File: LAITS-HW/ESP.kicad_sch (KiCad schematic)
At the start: 53 parts, among them J501 JTAG, SW501 SW_BOOT, SW502 SW_RST, SW503 SW_LOG_SD_EN, SW504 SW_RST_PROV, SW505 SW_RGB_CHRG, SW506 SW_SLEEP, U501 ESP32-WROVER-IE/E, U502 SX1503I091TRT

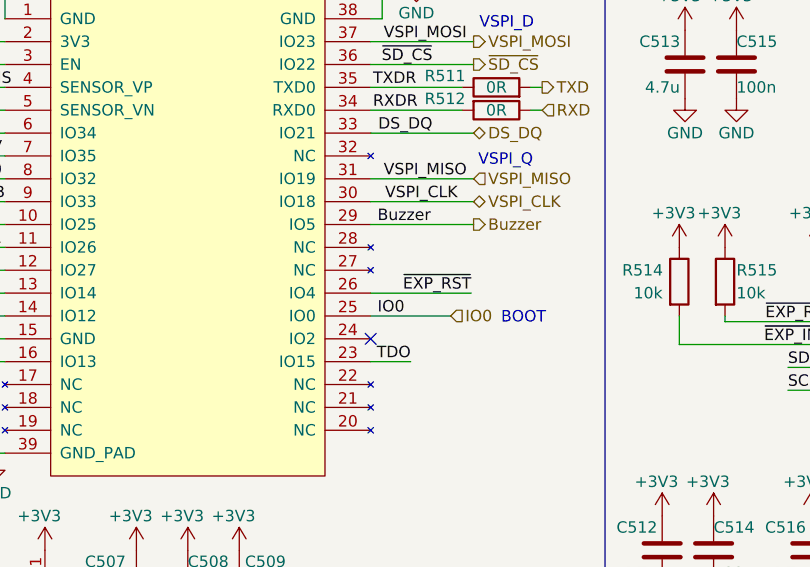
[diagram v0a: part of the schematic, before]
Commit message: improved silkscreen placement and some minor changes
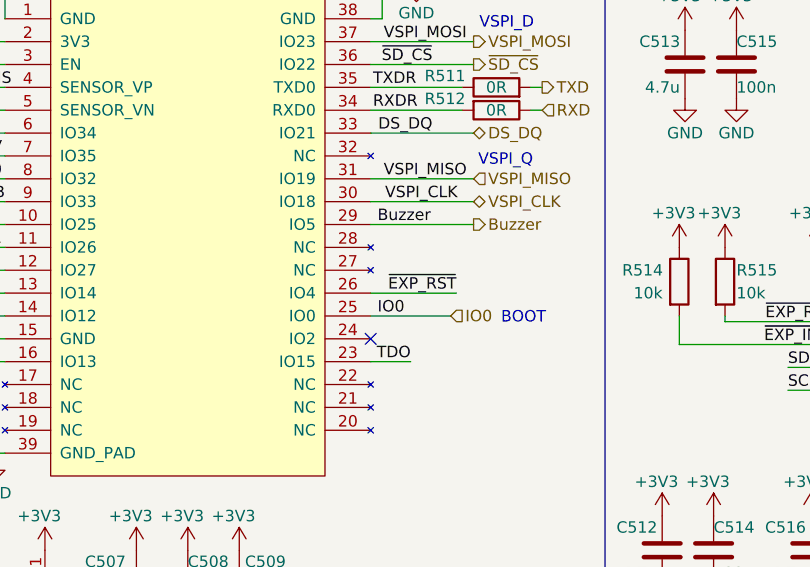
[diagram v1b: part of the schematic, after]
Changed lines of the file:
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@@
     (stroke (width 0) (type default) (color 0 0 0 0))
   )
-  (wire (pts (xy 161.29 59.69) (xy 172.466 59.69))
+  (wire (pts (xy 161.29 59.69) (xy 170.815 59.69))
     (stroke (width 0) (type default) (color 0 0 0 0))
   )
@@
     (effects (font (size 1.27 1.27)) (justify right bottom))
   )
-  (label "~{EXP_RST}" (at 172.466 59.69 180)
-    (effects (font (size 1.27 1.27)) (justify right bottom))
-  )
+  (label "~{EXP_RST}" (at 170.815 59.69 180)
+    (effects (font (size 1.27 1.27)) (justify right bottom))
+  )

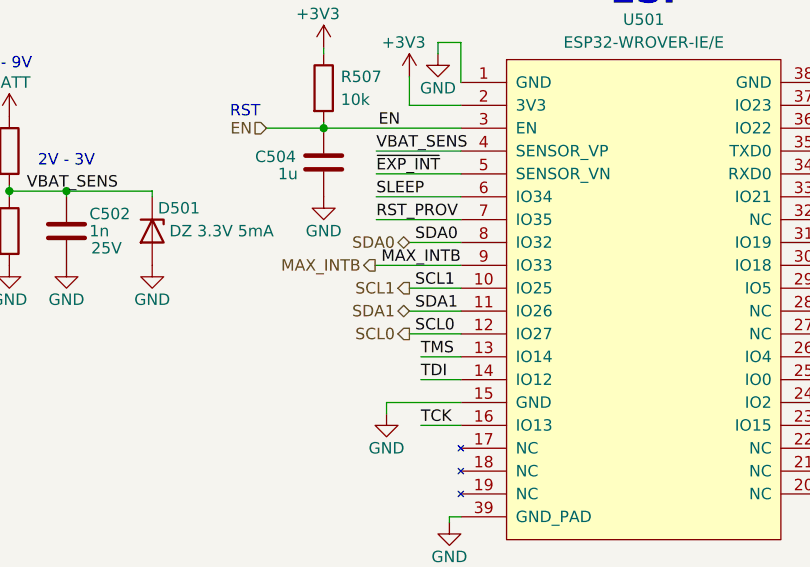
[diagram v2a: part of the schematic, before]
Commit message: Fixed a minor bug in the assignment of SDA0 and SCL0 pins, doesn't affect Hardware, swap in firmware
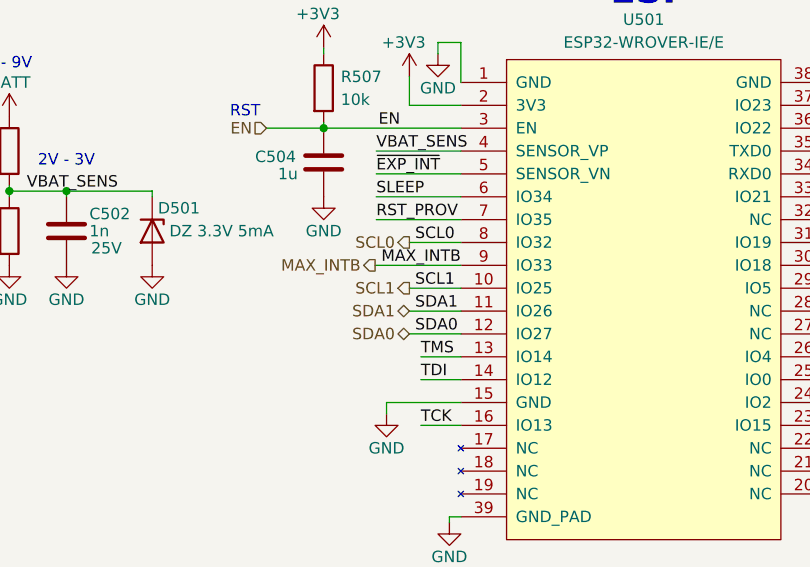
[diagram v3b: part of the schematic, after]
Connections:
- net SCL0: now also U501.8 (IO32); no longer U501.12 (IO27)
- net SDA0: now also U501.12 (IO27); no longer U501.8 (IO32)
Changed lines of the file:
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@@
   (title_block
     (title "ESP")
-    (date "2022-07-14")
-    (rev "1.0.1")
+    (date "2022-08-11")
+    (rev "1.0.2")
     (company "Simone Tollardo")
   )
@@
     (stroke (width 0) (type default) (color 0 0 0 0))
   )
+  (wire (pts (xy 114.935 57.15) (xy 120.65 57.15))
+    (stroke (width 0) (type default) (color 0 0 0 0))
+  )
   (wire (pts (xy 94.615 147.32) (xy 98.425 147.32))
     (stroke (width 0) (type default) (color 0 0 0 0))
@@
     (stroke (width 0) (type default) (color 0 0 0 0))
   )
+  (wire (pts (xy 120.65 24.765) (xy 120.65 29.21))
+    (stroke (width 0) (type default) (color 0 0 0 0))
+  )
+  (wire (pts (xy 154.305 147.32) (xy 154.305 150.495))
+    (stroke (width 0) (type default) (color 0 0 0 0))
+  )
+  (polyline (pts (xy 236.22 137.795) (xy 236.22 143.51))
+    (stroke (width 0) (type default) (color 0 0 0 0))
+  )
+  (wire (pts (xy 207.645 67.945) (xy 212.725 67.945))
+    (stroke (width 0) (type default) (color 0 0 0 0))
+  )
+  (wire (pts (xy 158.115 147.32) (xy 158.115 144.78))
+    (stroke (width 0) (type default) (color 0 0 0 0))
+  )
+  (wire (pts (xy 161.29 29.21) (xy 162.56 29.21))
+    (stroke (width 0) (type default) (color 0 0 0 0))
+  )
+  (wire (pts (xy 136.525 123.19) (xy 136.525 124.46))
+    (stroke (width 0) (type default) (color 0 0 0 0))
+  )
+  (wire (pts (xy 238.125 37.465) (xy 248.285 37.465))
+    (stroke (width 0) (type default) (color 0 0 0 0))
+  )
+  (polyline (pts (xy 187.325 163.83) (xy 187.325 102.235))
+    (stroke (width 0) (type default) (color 0 0 0 0))
+  )
+  (polyline (pts (xy 236.22 143.51) (xy 283.21 143.51))
+    (stroke (width 0) (type default) (color 0 0 0 0))
+  )
+  (polyline (pts (xy 62.865 163.83) (xy 62.865 194.31))
+    (stroke (width 0) (type default) (color 0 0 0 0))
+  )
+  (wire (pts (xy 235.585 36.83) (xy 235.585 45.085))
+    (stroke (width 0) (type default) (color 0 0 0 0))
+  )
+  (wire (pts (xy 73.66 136.525) (xy 73.66 133.35))
+    (stroke (width 0) (type default) (color 0 0 0 0))
+  )
+  (wire (pts (xy 132.08 147.32) (xy 134.62 147.32))
+    (stroke (width 0) (type default) (color 0 0 0 0))
+  )
+  (wire (pts (xy 235.585 81.28) (xy 238.125 81.28))
+    (stroke (width 0) (type default) (color 0 0 0 0))
+  )
+  (wire (pts (xy 243.205 41.275) (xy 243.205 45.085))
+    (stroke (width 0) (type default) (color 0 0 0 0))
+  )
+  (wire (pts (xy 247.65 41.275) (xy 243.205 41.275))
+    (stroke (width 0) (type default) (color 0 0 0 0))
+  )
+  (wire (pts (xy 154.305 147.32) (xy 158.115 147.32))
+    (stroke (width 0) (type default) (color 0 0 0 0))
+  )
+  (wire (pts (xy 172.085 147.32) (xy 174.625 147.32))
+    (stroke (width 0) (type default) (color 0 0 0 0))
+  )
+  (wire (pts (xy 37.465 67.31) (xy 37.465 69.85))
+    (stroke (width 0) (type default) (color 0 0 0 0))
+  )
+  (wire (pts (xy 156.21 123.19) (xy 156.21 124.46))
+    (stroke (width 0) (type default) (color 0 0 0 0))
+  )
+  (polyline (pts (xy 283.21 164.465) (xy 190.5 164.465))
+    (stroke (width 0) (type default) (color 0 0 0 0))
+  )
+  (wire (pts (xy 238.125 45.085) (xy 238.125 37.465))
+    (stroke (width 0) (type default) (color 0 0 0 0))
+  )
+  (polyline (pts (xy 236.22 143.51) (xy 236.22 156.845))
+    (stroke (width 0) (type default) (color 0 0 0 0))
+  )
+  (wire (pts (xy 236.22 36.83) (xy 235.585 36.83))
+    (stroke (width 0) (type default) (color 0 0 0 0))
+  )
+  (wire (pts (xy 31.115 121.285) (xy 38.735 121.285))
+    (stroke (width 0) (type default) (color 0 0 0 0))
+  )
+  (polyline (pts (xy 62.865 13.97) (xy 62.865 102.235))
+    (stroke (width 0) (type default) (color 0 0 0 0))
+  )
+  (wire (pts (xy 161.29 31.75) (xy 172.72 31.75))
+    (stroke (width 0) (type default) (color 0 0 0 0))
+  )
+  (wire (pts (xy 80.01 147.32) (xy 80.01 144.78))
+    (stroke (width 0) (type default) (color 0 0 0 0))
+  )
+  (wire (pts (xy 76.835 41.275) (xy 76.835 41.91))
+    (stroke (width 0) (type default) (color 0 0 0 0))
+  )
+  (wire (pts (xy 156.21 133.35) (xy 158.115 133.35))
+    (stroke (width 0) (type default) (color 0 0 0 0))
+  )
+  (polyline (pts (xy 13.97 13.97) (xy 13.97 102.235))
+    (stroke (width 0) (type default) (color 0 0 0 0))
+  )
+  (wire (pts (xy 99.06 34.29) (xy 105.41 34.29))
+    (stroke (width 0) (type default) (color 0 0 0 0))
+  )
+  (wire (pts (xy 73.66 144.145) (xy 73.66 147.32))
+    (stroke (width 0) (type default) (color 0 0 0 0))
+  )
+  (wire (pts (xy 132.08 144.145) (xy 132.08 147.32))
+    (stroke (width 0) (type default) (color 0 0 0 0))
+  )
+  (wire (pts (xy 31.115 118.745) (xy 38.735 118.745))
+    (stroke (width 0) (type default) (color 0 0 0 0))
+  )
   (wire (pts (xy 114.935 46.99) (xy 120.65 46.99))
-    (stroke (width 0) (type default) (color 0 0 0 0))
-  )
-  (wire (pts (xy 120.65 24.765) (xy 120.65 29.21))
-    (stroke (width 0) (type default) (color 0 0 0 0))
-  )
-  (wire (pts (xy 154.305 147.32) (xy 154.305 150.495))
-    (stroke (width 0) (type default) (color 0 0 0 0))
-  )
-  (polyline (pts (xy 236.22 137.795) (xy 236.22 143.51))
-    (stroke (width 0) (type default) (color 0 0 0 0))
-  )
-  (wire (pts (xy 207.645 67.945) (xy 212.725 67.945))
-    (stroke (width 0) (type default) (color 0 0 0 0))
-  )
-  (wire (pts (xy 158.115 147.32) (xy 158.115 144.78))
-    (stroke (width 0) (type default) (color 0 0 0 0))
-  )
-  (wire (pts (xy 161.29 29.21) (xy 162.56 29.21))
-    (stroke (width 0) (type default) (color 0 0 0 0))
-  )
-  (wire (pts (xy 136.525 123.19) (xy 136.525 124.46))
-    (stroke (width 0) (type default) (color 0 0 0 0))
-  )
-  (wire (pts (xy 238.125 37.465) (xy 248.285 37.465))
-    (stroke (width 0) (type default) (color 0 0 0 0))
-  )
-  (polyline (pts (xy 187.325 163.83) (xy 187.325 102.235))
-    (stroke (width 0) (type default) (color 0 0 0 0))
-  )
-  (polyline (pts (xy 236.22 143.51) (xy 283.21 143.51))
-    (stroke (width 0) (type default) (color 0 0 0 0))
-  )
-  (polyline (pts (xy 62.865 163.83) (xy 62.865 194.31))
-    (stroke (width 0) (type default) (color 0 0 0 0))
-  )
-  (wire (pts (xy 235.585 36.83) (xy 235.585 45.085))
-    (stroke (width 0) (type default) (color 0 0 0 0))
-  )
-  (wire (pts (xy 114.935 57.15) (xy 120.65 57.15))
-    (stroke (width 0) (type default) (color 0 0 0 0))
-  )
-  (wire (pts (xy 73.66 136.525) (xy 73.66 133.35))
-    (stroke (width 0) (type default) (color 0 0 0 0))
-  )
-  (wire (pts (xy 132.08 147.32) (xy 134.62 147.32))
-    (stroke (width 0) (type default) (color 0 0 0 0))
-  )
-  (wire (pts (xy 235.585 81.28) (xy 238.125 81.28))
-    (stroke (width 0) (type default) (color 0 0 0 0))
-  )
-  (wire (pts (xy 243.205 41.275) (xy 243.205 45.085))
-    (stroke (width 0) (type default) (color 0 0 0 0))
-  )
-  (wire (pts (xy 247.65 41.275) (xy 243.205 41.275))
-    (stroke (width 0) (type default) (color 0 0 0 0))
-  )
-  (wire (pts (xy 154.305 147.32) (xy 158.115 147.32))
-    (stroke (width 0) (type default) (color 0 0 0 0))
-  )
-  (wire (pts (xy 172.085 147.32) (xy 174.625 147.32))
-    (stroke (width 0) (type default) (color 0 0 0 0))
-  )
-  (wire (pts (xy 37.465 67.31) (xy 37.465 69.85))
-    (stroke (width 0) (type default) (color 0 0 0 0))
-  )
-  (wire (pts (xy 156.21 123.19) (xy 156.21 124.46))
-    (stroke (width 0) (type default) (color 0 0 0 0))
-  )
-  (polyline (pts (xy 283.21 164.465) (xy 190.5 164.465))
-    (stroke (width 0) (type default) (color 0 0 0 0))
-  )
-  (wire (pts (xy 238.125 45.085) (xy 238.125 37.465))
-    (stroke (width 0) (type default) (color 0 0 0 0))
-  )
-  (polyline (pts (xy 236.22 143.51) (xy 236.22 156.845))
-    (stroke (width 0) (type default) (color 0 0 0 0))
-  )
-  (wire (pts (xy 236.22 36.83) (xy 235.585 36.83))
-    (stroke (width 0) (type default) (color 0 0 0 0))
-  )
-  (wire (pts (xy 31.115 121.285) (xy 38.735 121.285))
-    (stroke (width 0) (type default) (color 0 0 0 0))
-  )
-  (polyline (pts (xy 62.865 13.97) (xy 62.865 102.235))
-    (stroke (width 0) (type default) (color 0 0 0 0))
-  )
-  (wire (pts (xy 161.29 31.75) (xy 172.72 31.75))
-    (stroke (width 0) (type default) (color 0 0 0 0))
-  )
-  (wire (pts (xy 80.01 147.32) (xy 80.01 144.78))
-    (stroke (width 0) (type default) (color 0 0 0 0))
-  )
-  (wire (pts (xy 76.835 41.275) (xy 76.835 41.91))
-    (stroke (width 0) (type default) (color 0 0 0 0))
-  )
-  (wire (pts (xy 156.21 133.35) (xy 158.115 133.35))
-    (stroke (width 0) (type default) (color 0 0 0 0))
-  )
-  (polyline (pts (xy 13.97 13.97) (xy 13.97 102.235))
-    (stroke (width 0) (type default) (color 0 0 0 0))
-  )
-  (wire (pts (xy 99.06 34.29) (xy 105.41 34.29))
-    (stroke (width 0) (type default) (color 0 0 0 0))
-  )
-  (wire (pts (xy 73.66 144.145) (xy 73.66 147.32))
-    (stroke (width 0) (type default) (color 0 0 0 0))
-  )
-  (wire (pts (xy 132.08 144.145) (xy 132.08 147.32))
-    (stroke (width 0) (type default) (color 0 0 0 0))
-  )
-  (wire (pts (xy 31.115 118.745) (xy 38.735 118.745))
     (stroke (width 0) (type default) (color 0 0 0 0))
   )
@@
     (effects (font (size 1.27 1.27)) (justify right bottom))
   )
-  (label "SDA0" (at 115.57 46.99 0)
+  (label "SDA0" (at 115.57 57.15 0)
     (effects (font (size 1.27 1.27)) (justify left bottom))
   )
@@
     (effects (font (size 1.27 1.27)) (justify right bottom))
   )
-  (label "SCL0" (at 115.57 57.15 0)
+  (label "SCL0" (at 115.57 46.99 0)
     (effects (font (size 1.27 1.27)) (justify left bottom))
   )
@@
     (effects (font (size 1.27 1.27)) (justify left))
   )
-  (hierarchical_label "SCL0" (shape output) (at 114.935 57.15 180)
+  (hierarchical_label "SCL0" (shape output) (at 114.935 46.99 180)
     (effects (font (size 1.27 1.27)) (justify right))
   )
@@
     (effects (font (size 1.27 1.27)) (justify left))
   )
-  (hierarchical_label "SDA0" (shape bidirectional) (at 114.935 46.99 180)
+  (hierarchical_label "SDA0" (shape bidirectional) (at 114.935 57.15 180)
     (effects (font (size 1.27 1.27)) (justify right))
   )

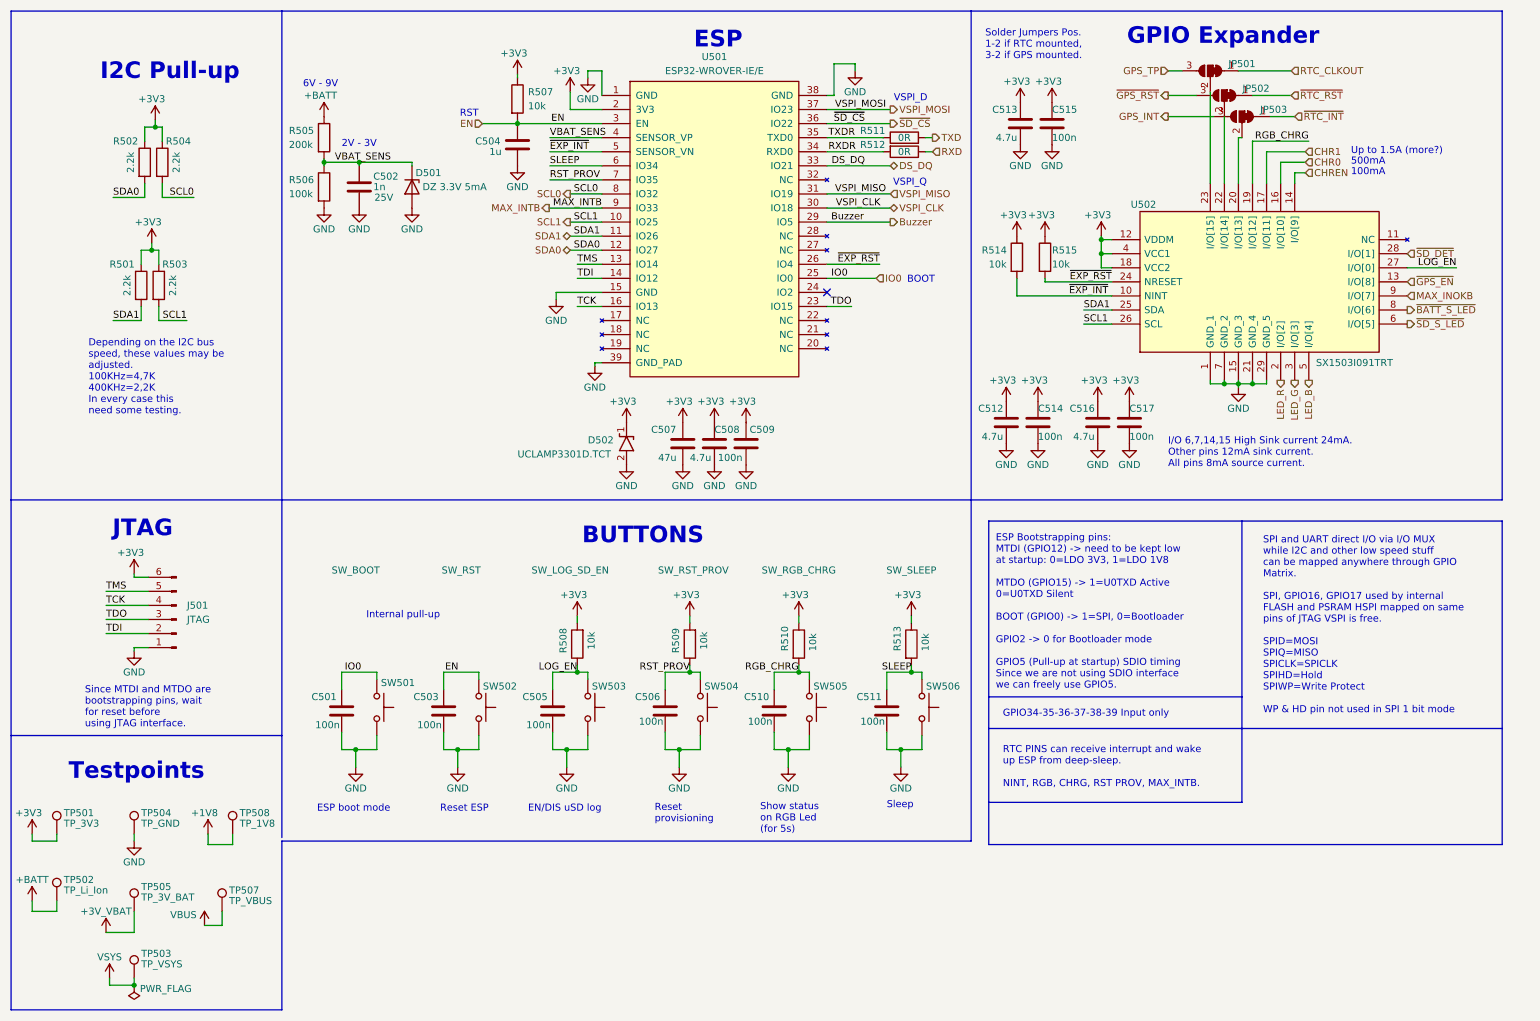
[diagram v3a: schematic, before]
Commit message: Now LAITS notify charge state also when turned off
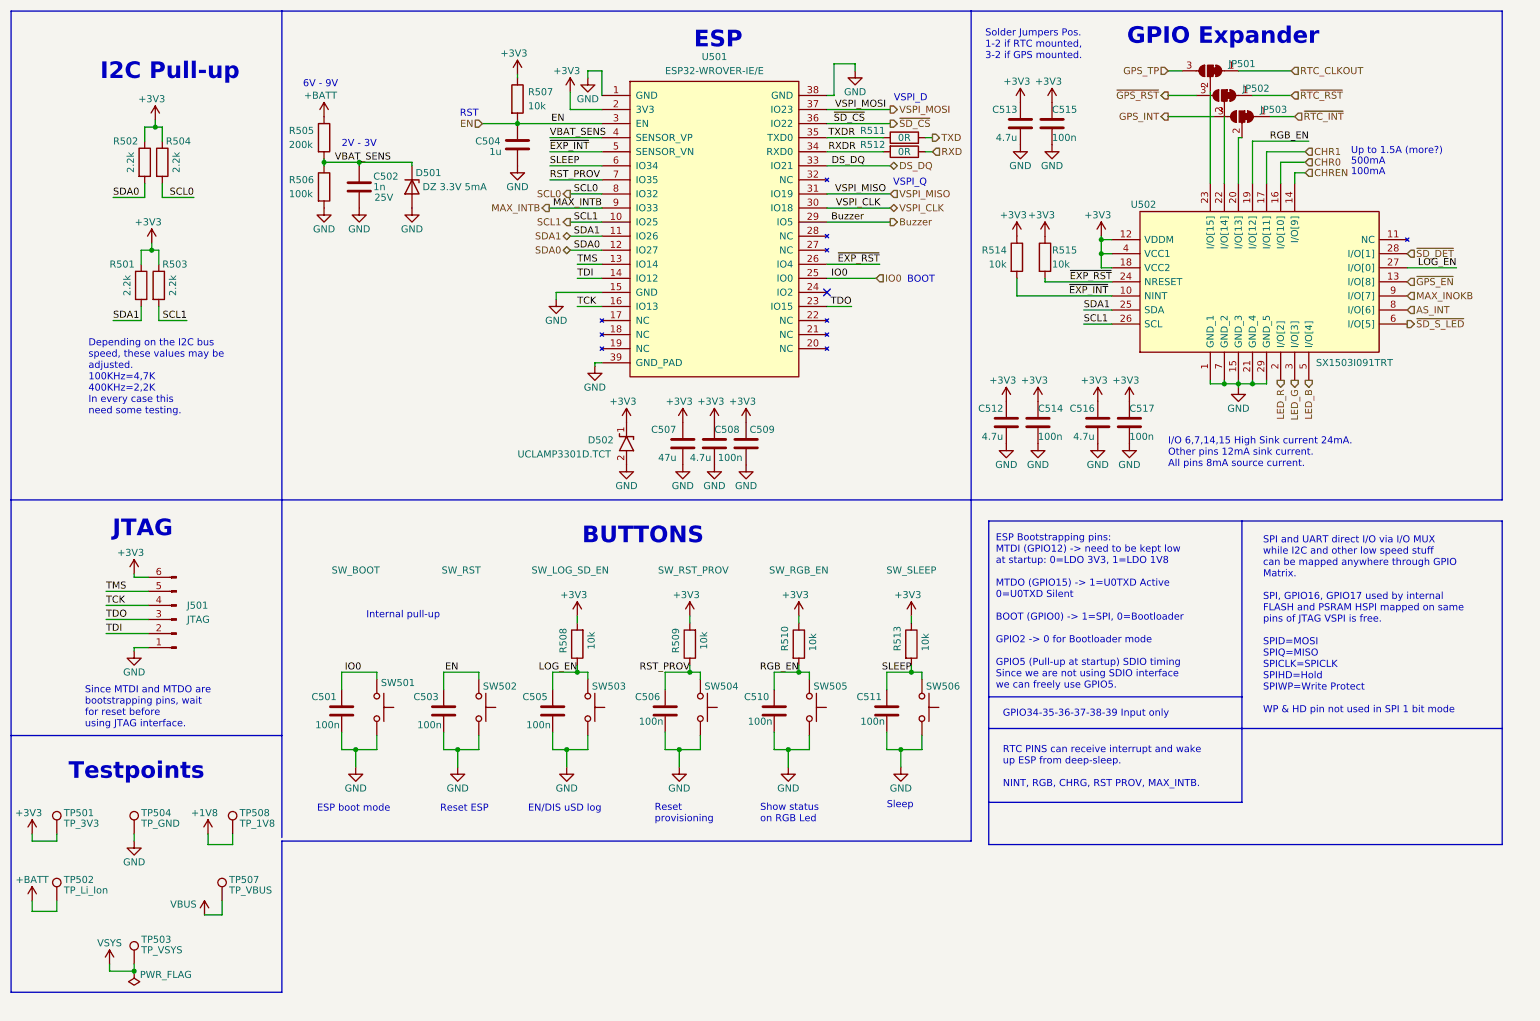
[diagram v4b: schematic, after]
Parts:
- removed TP505: TP_3V_BAT, TestPoint:TestPoint_THTPad_D1.5mm_Drill0.7mm, symbol Connector:TestPoint
- SW501, SW502: footprint Button_Switch_THT:SW_Tactile_SPST_Angled_PTS645Vx83-2LFS -> Button_Switch_THT:SW_PUSH_6mm_H5mm
- SW505: value SW_RGB_CHRG -> SW_RGB_EN
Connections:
- net RGB_CHRG renamed RGB_EN
- net ~{BATT_S_LED} renamed AS_INT
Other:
- note added: "Show status on RGB Led"
- note removed: "Show status on RGB Led (for 5s)"
- moved on the sheet: TP503, TP507
